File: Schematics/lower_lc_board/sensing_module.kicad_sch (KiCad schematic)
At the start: 26 parts, among them J4 HALL-1, J5 HALL-2, Q3 2N7002, U11 DMP4065S-7, U9 ADC_ADS131M04IPWR

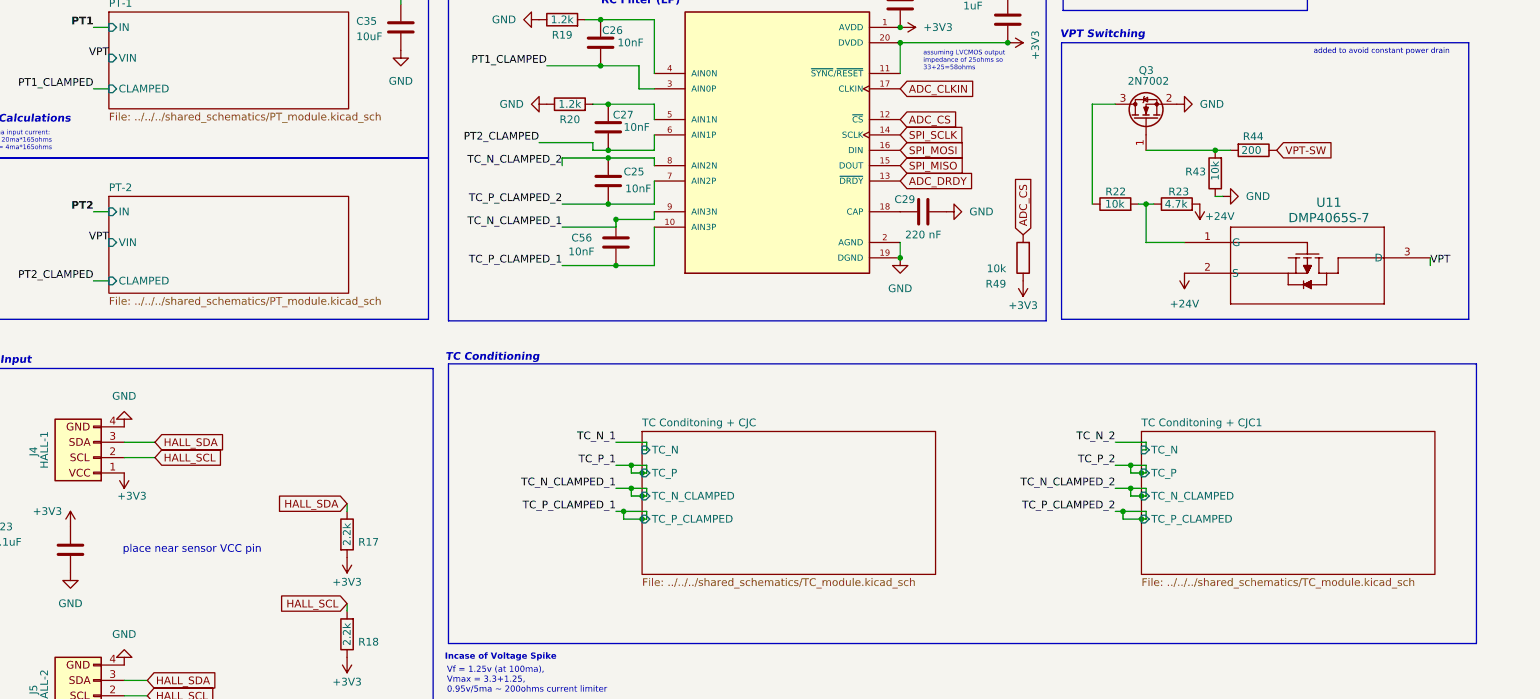
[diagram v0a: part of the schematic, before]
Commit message: organize working copy of lower valve board for merge to main
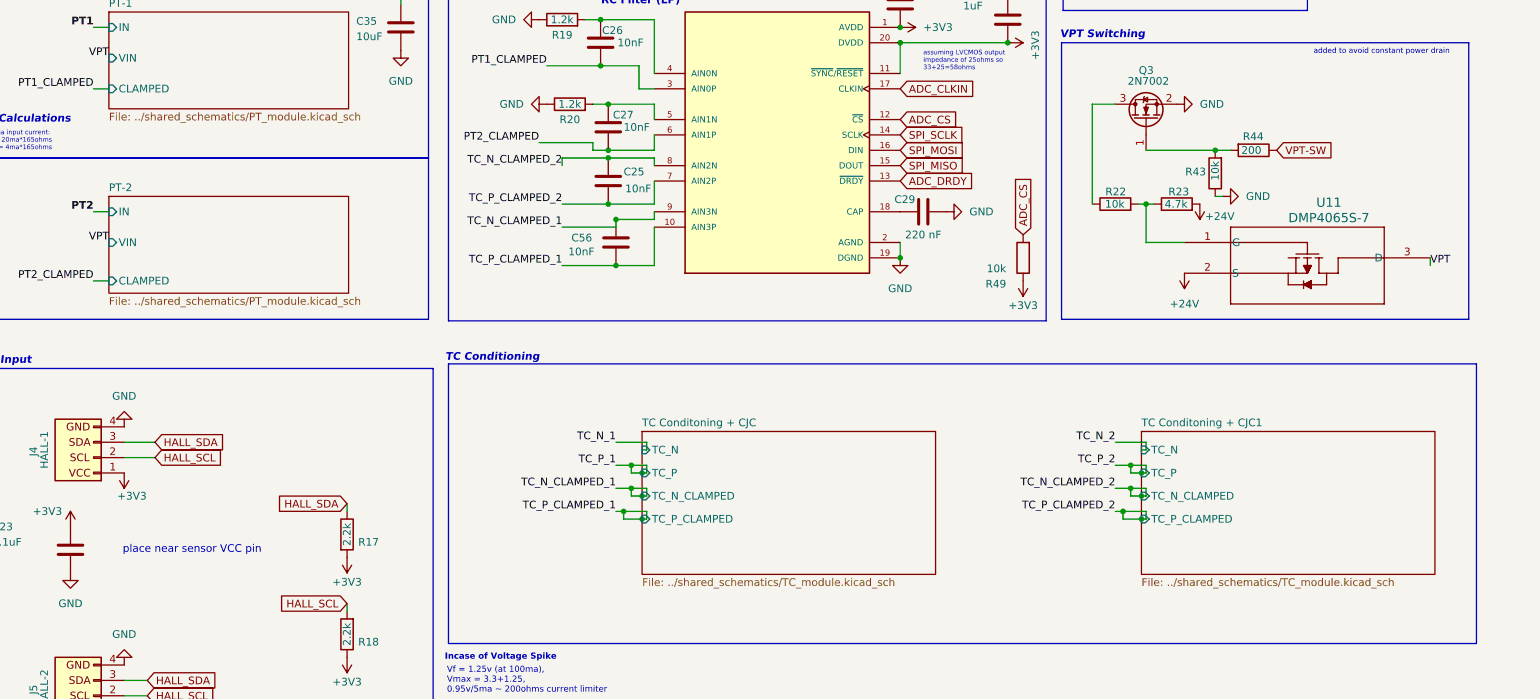
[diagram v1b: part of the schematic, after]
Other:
- sheet PT-1: file ../../../shared_schematics/PT_module.kicad_sch -> ../shared_schematics/PT_module.kicad_sch
- sheet PT-2: file ../../../shared_schematics/PT_module.kicad_sch -> ../shared_schematics/PT_module.kicad_sch
- sheet TC Conditoning + CJC: file ../../../shared_schematics/TC_module.kicad_sch -> ../shared_schematics/TC_module.kicad_sch
- sheet TC Conditoning + CJC1: file ../../../shared_schematics/TC_module.kicad_sch -> ../shared_schematics/TC_module.kicad_sch
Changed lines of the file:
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@@
 	(label "TC_P_1"
 		(at 135.89 116.84 180)
-		(fields_autoplaced yes)
 		(effects
 			(font
@@
 	(label "TC_N_CLAMPED_1"
 		(at 135.89 120.65 180)
-		(fields_autoplaced yes)
 		(effects
 			(font
@@
 	(label "TC_N_2"
 		(at 218.44 113.03 180)
-		(fields_autoplaced yes)
 		(effects
 			(font
@@
 	(label "TC_N_CLAMPED_2"
 		(at 127 67.31 180)
-		(fields_autoplaced yes)
 		(effects
 			(font
@@
 	(label "PT1_CLAMPED"
 		(at 124.46 50.8 180)
-		(fields_autoplaced yes)
 		(effects
 			(font
@@
 	(label "TC_N_1"
 		(at 135.89 113.03 180)
-		(fields_autoplaced yes)
 		(effects
 			(font
@@
 	(label "TC_P_2"
 		(at 218.44 116.84 180)
-		(fields_autoplaced yes)
 		(effects
 			(font
@@
 	(label "PT2"
 		(at 49.53 74.93 180)
-		(fields_autoplaced yes)
 		(effects
 			(font
@@
 	(label "TC_N_CLAMPED_2"
 		(at 218.44 120.65 180)
-		(fields_autoplaced yes)
 		(effects
 			(font
@@
 	(label "TC_P_CLAMPED_2"
 		(at 127 73.66 180)
-		(fields_autoplaced yes)
 		(effects
 			(font
@@
 	(label "VPT"
 		(at 52.07 49.53 180)
-		(fields_autoplaced yes)
 		(effects
 			(font
@@
 	(label "VPT"
 		(at 52.07 80.01 180)
-		(fields_autoplaced yes)
 		(effects
 			(font
@@
 	(label "PT2_CLAMPED"
 		(at 123.19 63.5 180)
-		(fields_autoplaced yes)
 		(effects
 			(font
@@
 	(label "VPT"
 		(at 100.33 39.37 180)
-		(fields_autoplaced yes)
 		(effects
 			(font
@@
 	(label "PT1_CLAMPED"
 		(at 49.53 54.61 180)
-		(fields_autoplaced yes)
 		(effects
 			(font
@@
 	(label "TC_N_CLAMPED_1"
 		(at 127 77.47 180)
-		(fields_autoplaced yes)
 		(effects
 			(font
@@
 	(label "PT1"
 		(at 49.53 44.45 180)
-		(fields_autoplaced yes)
 		(effects
 			(font
@@
 	(label "TC_P_CLAMPED_1"
 		(at 135.89 124.46 180)
-		(fields_autoplaced yes)
 		(effects
 			(font
@@
 	(label "PT2_CLAMPED"
 		(at 49.53 86.36 180)
-		(fields_autoplaced yes)
 		(effects
 			(font
@@
 	(label "VPT"
 		(at 270.51 83.82 0)
-		(fields_autoplaced yes)
 		(effects
 			(font
@@
 	(label "TC_P_CLAMPED_2"
 		(at 218.44 124.46 180)
-		(fields_autoplaced yes)
 		(effects
 			(font
@@
 	(label "TC_P_CLAMPED_1"
 		(at 127 83.82 180)
-		(fields_autoplaced yes)
 		(effects
 			(font
@@
 			)
 		)
-		(property "Datasheet" "${KIPRJMOD}/../../Documentation/nmosfet_2N7002_DS.PDF"
+		(property "Datasheet" "${KIPRJMOD}/../../Datasheets/nmosfet_2N7002_DS.PDF"
 			(at 227.33 54.61 0)
 			(effects
@@
 		)
 		(instances
-			(project ""
+			(project "lower_lc_board"
 				(path "/d63798c4-e363-437e-9012-e4aff32e6642/c6419db7-28a9-4bfa-8244-fc88166c795c"
 					(reference "Q3")
@@
 		)
 		(instances
-			(project ""
+			(project "lower_lc_board"
 				(path "/d63798c4-e363-437e-9012-e4aff32e6642/c6419db7-28a9-4bfa-8244-fc88166c795c"
 					(reference "#PWR063")
@@
 		)
 		(instances
-			(project ""
+			(project "lower_lc_board"
 				(path "/d63798c4-e363-437e-9012-e4aff32e6642/c6419db7-28a9-4bfa-8244-fc88166c795c"
 					(reference "#PWR084")
@@
 			)
 		)
-		(property "Datasheet" "${KIPRJMOD}/../../Documentation/thermistor_tx_DS.pdf"
+		(property "Datasheet" "${KIPRJMOD}/../../Datasheets/thermistor_tx_DS.pdf"
 			(at 130.81 177.8 0)
 			(effects
@@
 			)
 		)
-		(property "Datasheet" "${KIPRJMOD}/../../Documentation/pmosfet_DMP4065S-7_DS.pdf"
+		(property "Datasheet" "${KIPRJMOD}/../../Datasheets/pmosfet_DMP4065S-7_DS.pdf"
 			(at 229.87 80.01 0)
 			(effects
@@
 		)
 		(instances
-			(project ""
+			(project "lower_lc_board"
 				(path "/d63798c4-e363-437e-9012-e4aff32e6642/c6419db7-28a9-4bfa-8244-fc88166c795c"
 					(reference "U11")
@@
 		)
 		(instances
-			(project ""
+			(project "lower_lc_board"
 				(path "/d63798c4-e363-437e-9012-e4aff32e6642/c6419db7-28a9-4bfa-8244-fc88166c795c"
 					(reference "R22")
@@
 			)
 		)
-		(property "Datasheet" "${KIPRJMOD}/../../Documentation/ADC_ads131m04_DS.pdf"
+		(property "Datasheet" "${KIPRJMOD}/../../Datasheets/ADC_ads131m04_DS.pdf"
 			(at 162.56 64.77 0)
 			(effects
@@
 			)
 		)
-		(property "Sheetfile" "../../../shared_schematics/PT_module.kicad_sch"
+		(property "Sheetfile" "../shared_schematics/PT_module.kicad_sch"
 			(at 52.07 88.9766 0)
 			(effects
@@
 			)
 		)
-		(property "Sheetfile" "../../../shared_schematics/TC_module.kicad_sch"
+		(property "Sheetfile" "../shared_schematics/TC_module.kicad_sch"
 			(at 140.208 135.4586 0)
 			(effects
@@
 			)
 		)
-		(property "Sheetfile" "../../../shared_schematics/TC_module.kicad_sch"
+		(property "Sheetfile" "../shared_schematics/TC_module.kicad_sch"
 			(at 222.758 135.4586 0)
 			(effects
@@
 			)
 		)
-		(property "Sheetfile" "../../../shared_schematics/PT_module.kicad_sch"
+		(property "Sheetfile" "../shared_schematics/PT_module.kicad_sch"
 			(at 52.07 58.4966 0)
 			(effects

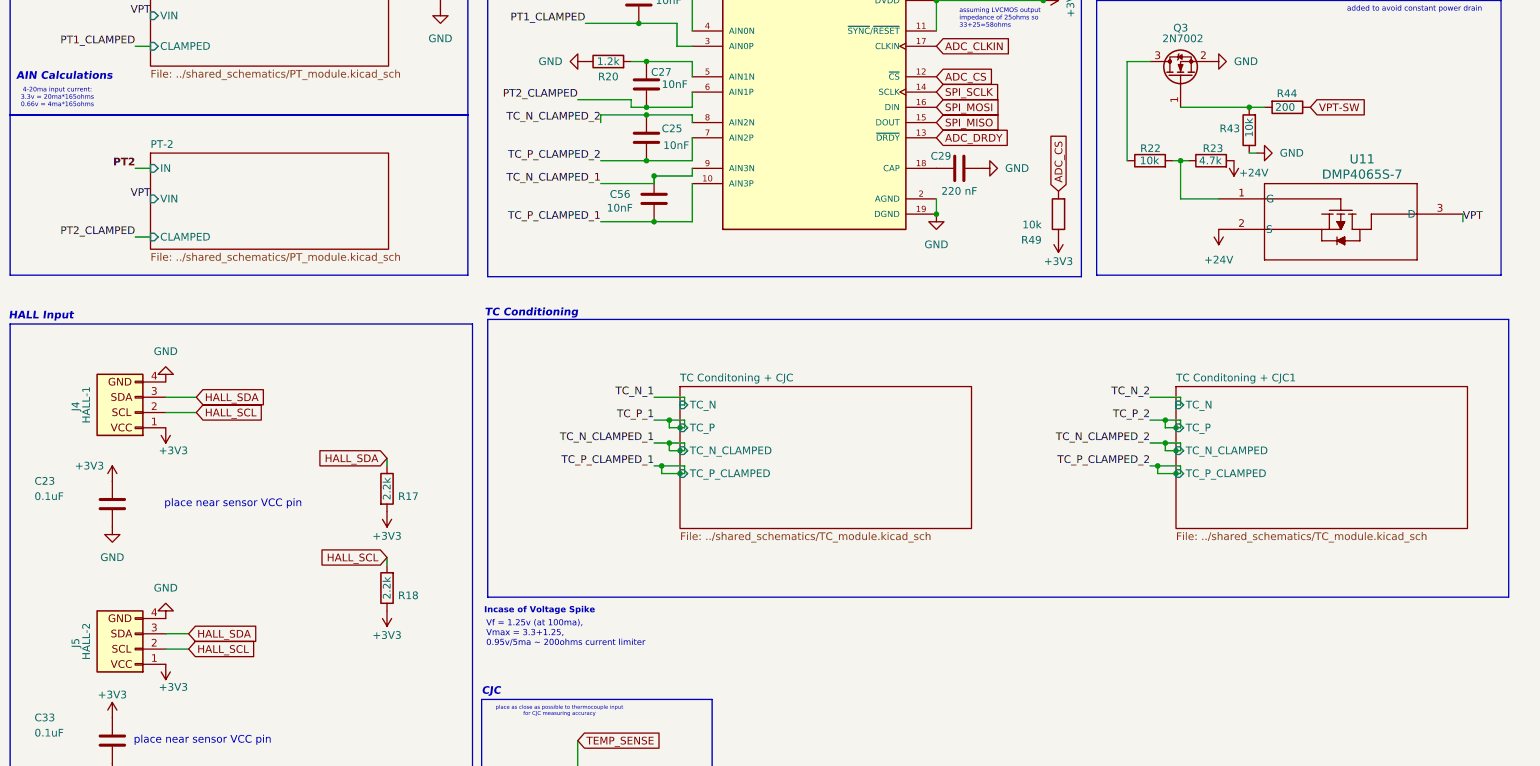
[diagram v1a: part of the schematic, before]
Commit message: lower refactor for review
 - curr using horziontal screw for TC
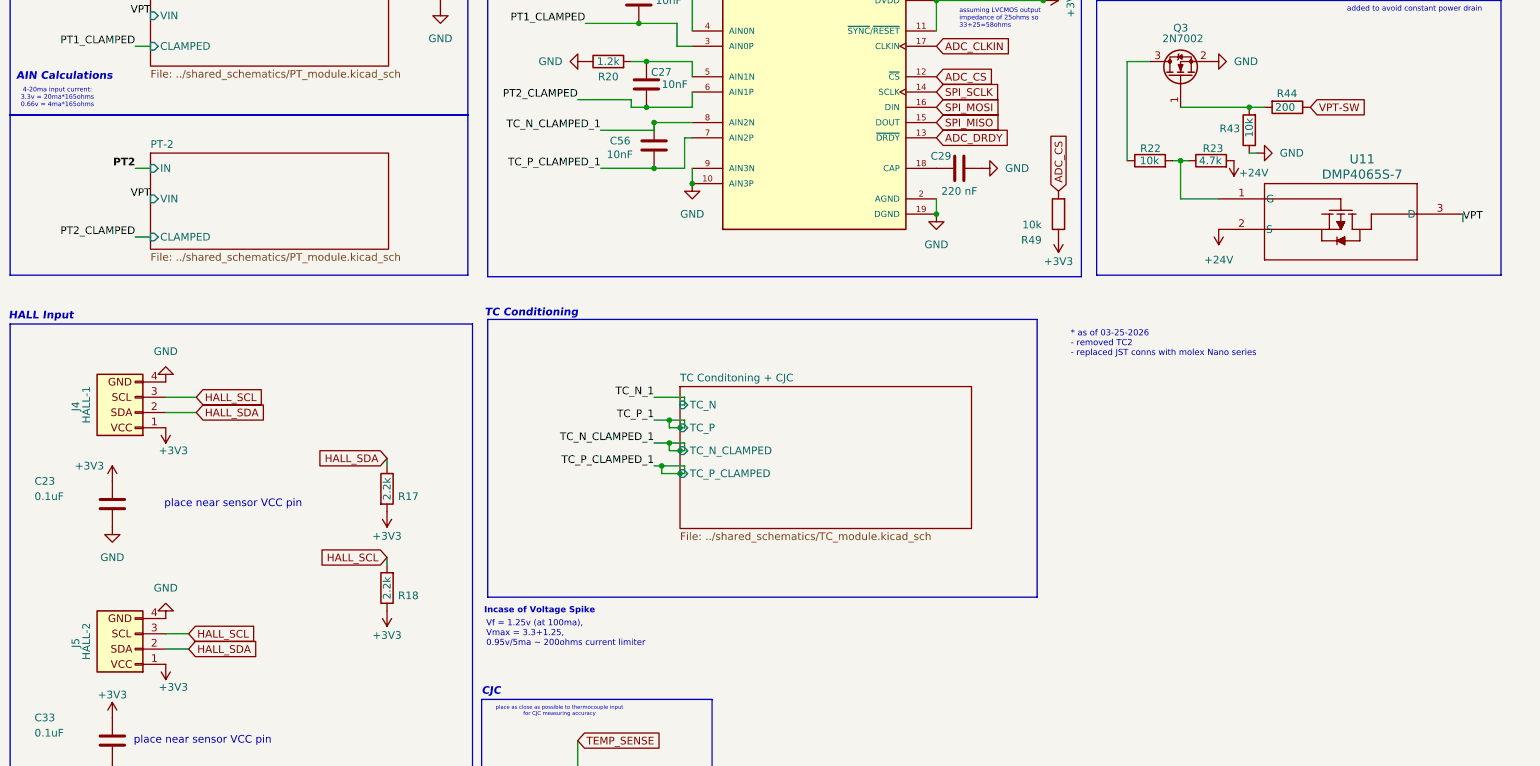
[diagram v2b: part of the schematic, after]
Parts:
- removed C25: 10nF, Capacitor_SMD:C_0603_1608Metric, symbol Device:C
- J4, J5: footprint S04B_PASK_2-P:CONN4_S04B-PASK_JST -> NANO-H-4-CONN:CONN_SD-105313-100_04_MOL; Digikey 455-S04B-PASK-2-ND -> WM16895-ND
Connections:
- net TC_N_CLAMPED_2 is gone; now on net TC_N_CLAMPED_1: U9.8 (AIN2N)
- net TC_P_CLAMPED_2 is gone; now on net TC_P_CLAMPED_1: U9.7 (AIN2P)
- net GND: now also U9.10 (AIN3P), U9.9 (AIN3N)
- net HALL_SCL: now also J4.3 (Pin_3), J5.3 (Pin_3); no longer J4.2 (Pin_2), J5.2 (Pin_2)
- net HALL_SDA: now also J4.2 (Pin_2), J5.2 (Pin_2); no longer J4.3 (Pin_3), J5.3 (Pin_3)
- net TC_N_CLAMPED_1: no longer U9.9 (AIN3N)
- net TC_P_CLAMPED_1: no longer U9.10 (AIN3P)
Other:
- removed sheet TC Conditoning + CJC1
- note added: "* as of 03-25-2026 - removed TC2 - replaced JST conns with molex Nano series"
- moved on the sheet: C56

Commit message: update backplane orientation
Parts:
- Q3: LCSC (none) -> C8545
- U11: Digikey C182476 -> (none); JLCPCB (none) -> C182476; LCSC (none) -> C182476
